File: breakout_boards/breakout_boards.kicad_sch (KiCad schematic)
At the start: 53 parts, among them J1 USB_C_Receptacle_USB2.0, J2 USB_POWER_HEADER, J3 USB_POWER_HEADER_2, J4 ANALOG RGB HEADER, J5 ADDRESSIBLE RGB HEADER 1, J6 ADDRESSIBLE RGB HEADER 2, Q1 AO3400A, Q2 AO3400A, Q3 AO3400A, U1 CH340C, U2 IP2721, U3 XC6210B332MR, U5 MT1470, U6 ESP-12F

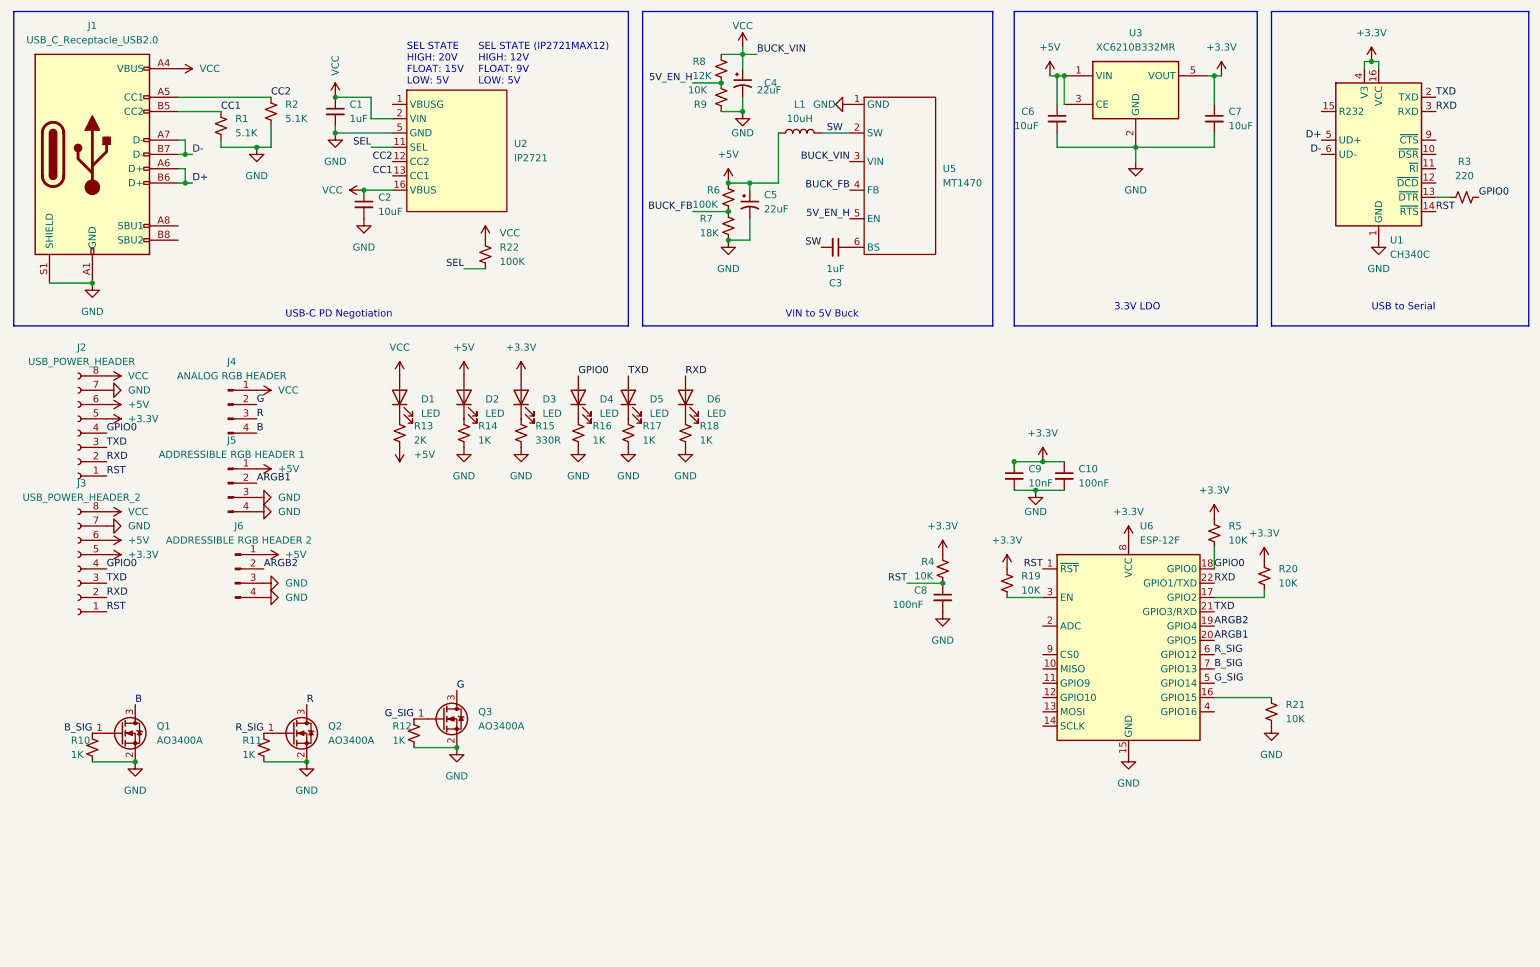
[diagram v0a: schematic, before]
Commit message: V2.1
Increased current capacity, changed modules to be 30V tolerant
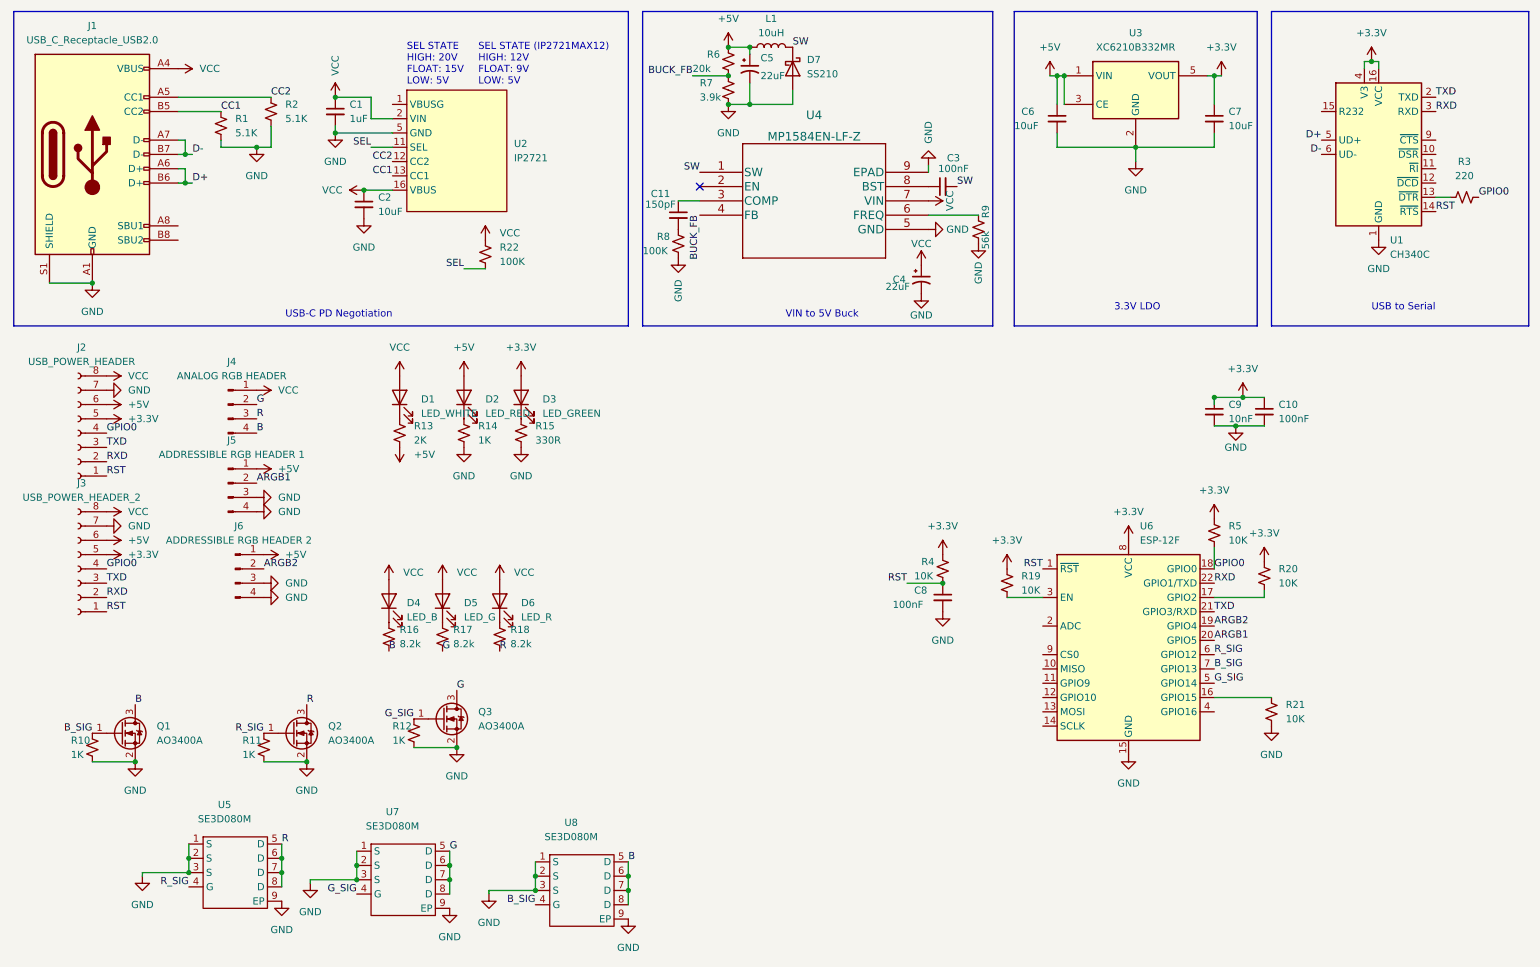
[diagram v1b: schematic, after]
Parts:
- removed U5: MT1470, Package_TO_SOT_SMD:TSOT-23-6, symbol MT1470:MT1470
- added C11: 150pF, Capacitor_SMD:C_0402_1005Metric, symbol Device:C_Small
- added D7: SS210, Diode_SMD:D_SMA, symbol Diode:B120-E3
- added U4: MP1584EN-LF-Z, Package_SO:SOIC-8-1EP_3.9x4.9mm_P1.27mm_EP2.62x3.51mm, symbol MP1584:MP1584EN-LF-Z
- added U5, U7, U8: SE3D080M, Package_DFN_QFN:DFN-8-1EP_3x3mm_P0.65mm_EP1.55x2.4mm, symbol SE3D080M:SE3D080M
- C3: value 1uF -> 100nF; LCSC C52923 -> C1525
- D1: value LED -> LED_WHITE
- D2: value LED -> LED_RED
- D3: value LED -> LED_GREEN
- D4: value LED -> LED_B; LCSC C72041 -> C72043; LCSC Part Number C2286 -> C72043
- D5: value LED -> LED_G; LCSC C2286 -> C72043; LCSC Part Number C2286 -> C72043
- D6: value LED -> LED_R; LCSC C2286 -> C72043; LCSC Part Number C2286 -> C72043
- R16, R17, R18: value 1K -> 8.2k; LCSC C11702 -> C25104; LCSC Part Number C11702 -> C25104
- R6: value 100K -> 20k
- R7: value 18K -> 3.9k
- R8: value 12K -> 100K; LCSC C25752 -> C25741; LCSC Part Number C25752 -> C25741
- R9: value 10K -> 56k; LCSC C25744 -> C25796; LCSC Part Number C25744 -> (none)
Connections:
- net B: now also R16.2, U8.5 (D), U8.6 (D), U8.7 (D), U8.8 (D)
- net BUCK_FB: now also U4.4 (FB)
- net B_SIG: now also U8.4 (G)
- net G: now also R17.2, U7.5 (D), U7.6 (D), U7.7 (D), U7.8 (D)
- net GND: now also R8.2, R9.2, D7.2 (A), U4.5 (GND), U4.9 (EPAD), U5.1 (S), U5.2 (S), U5.3 (S), U5.9 (EP), U7.1 (S), U7.2 (S), U7.3 (S), U7.9 (EP), U8.1 (S), U8.2 (S), U8.3 (S), U8.9 (EP); no longer R16.2, R17.2, R18.2, R9.1
- net GPIO0: no longer D4.2 (A)
- net G_SIG: now also U7.4 (G)
- net R: now also R18.2, U5.5 (D), U5.6 (D), U5.7 (D), U5.8 (D)
- net RXD: no longer D6.2 (A)
- net R_SIG: now also U5.4 (G)
- net SW: now also D7.1 (K), U4.1 (SW)
- net TXD: no longer D5.2 (A)
- net VCC: now also D4.2 (A), D5.2 (A), D6.2 (A), U4.7 (VIN); no longer R8.2
- net at C3.1: now also U4.8 (BST)
- net 5V_EN_H: no longer names the net of R8.1
- net 5V_EN_H: now also C11.2; no longer R9.2
- new net: C11.1, U4.3 (COMP)
- new net: R9.1, U4.6 (FREQ)
- no-connect marks 0 -> 1
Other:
- moved on the sheet: C10, C3, C4, C5, C9, L1, R6, R7
